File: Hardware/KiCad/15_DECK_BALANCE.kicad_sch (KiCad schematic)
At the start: 0 parts

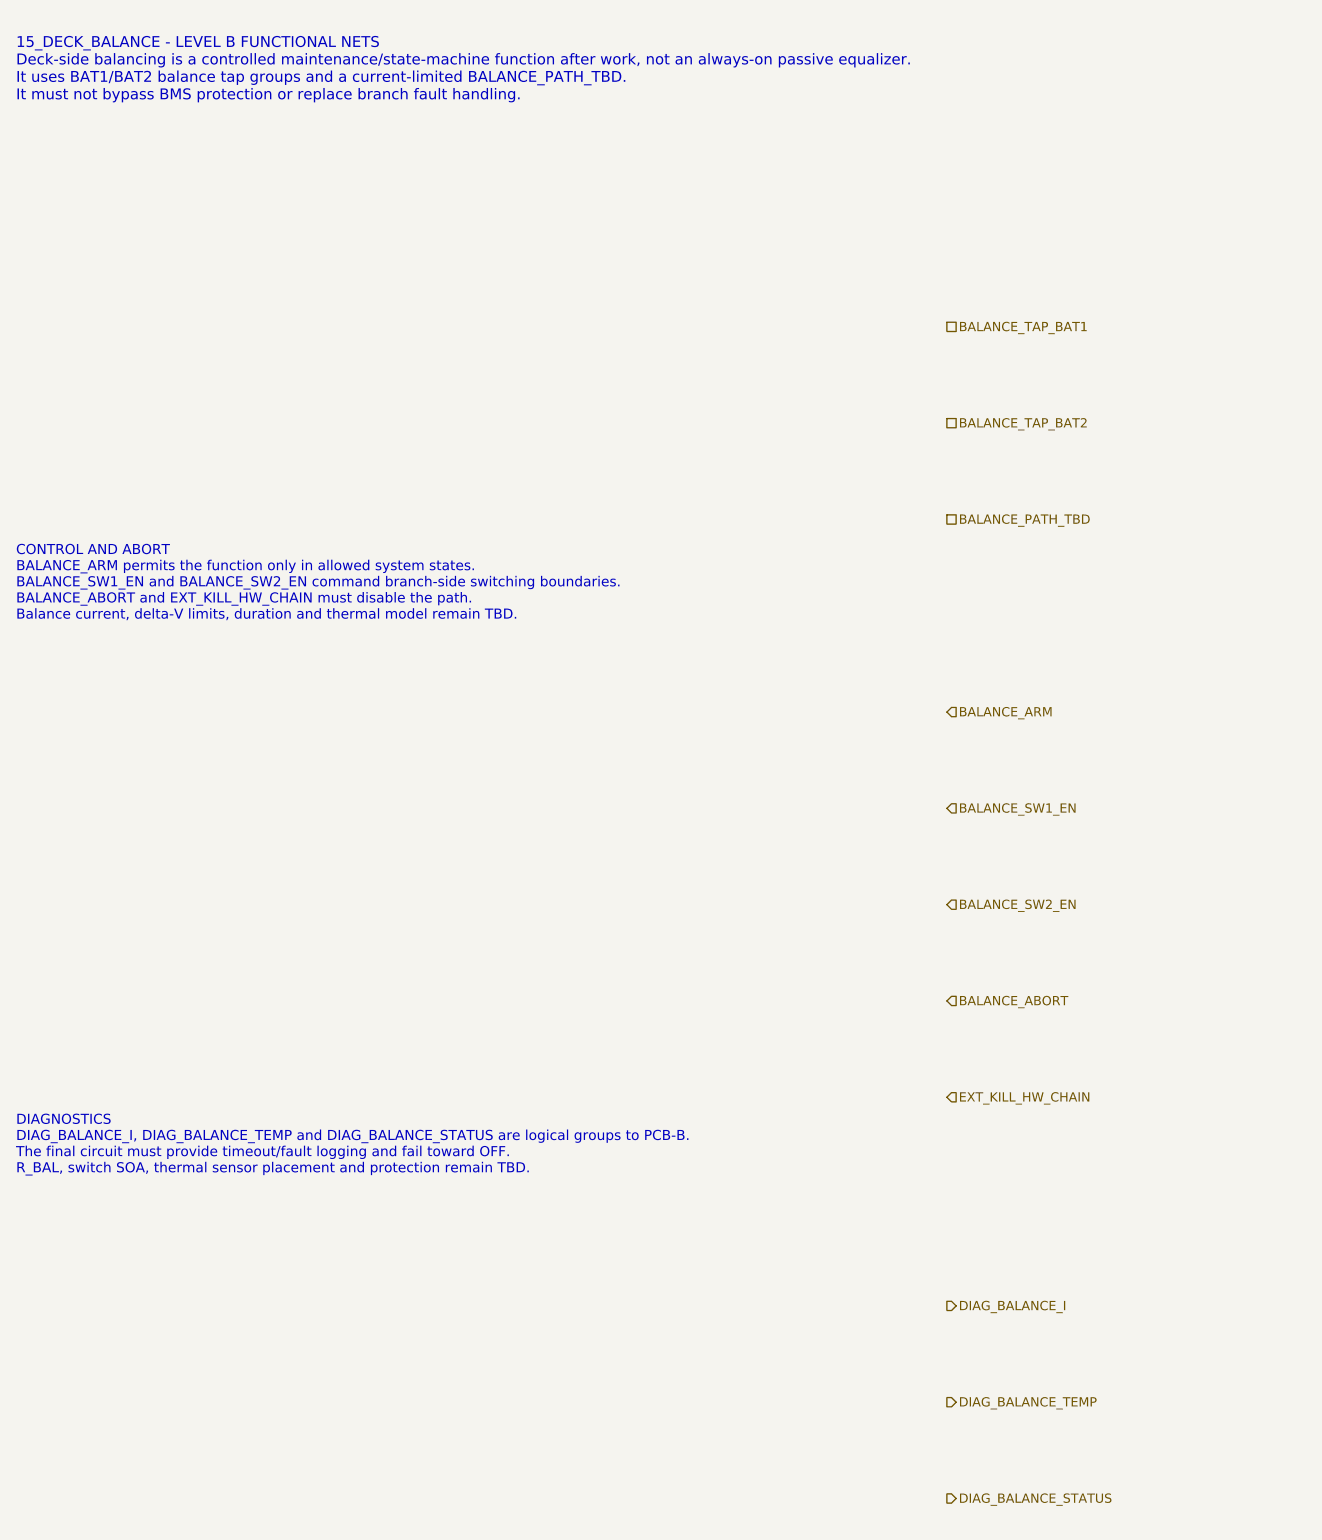
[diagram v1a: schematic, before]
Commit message: hardware: add remaining BFE symbol skeleton zones
Complete text-only symbol skeleton zones for remaining PCB-A BFE_POWER sheets.

Includes PACK_BUS, MAIN paths, measurements, deck balance, connectors and testpoints.
No real KiCad library symbols, part numbers, footprints, BOM entries or PCB layout are introduced.
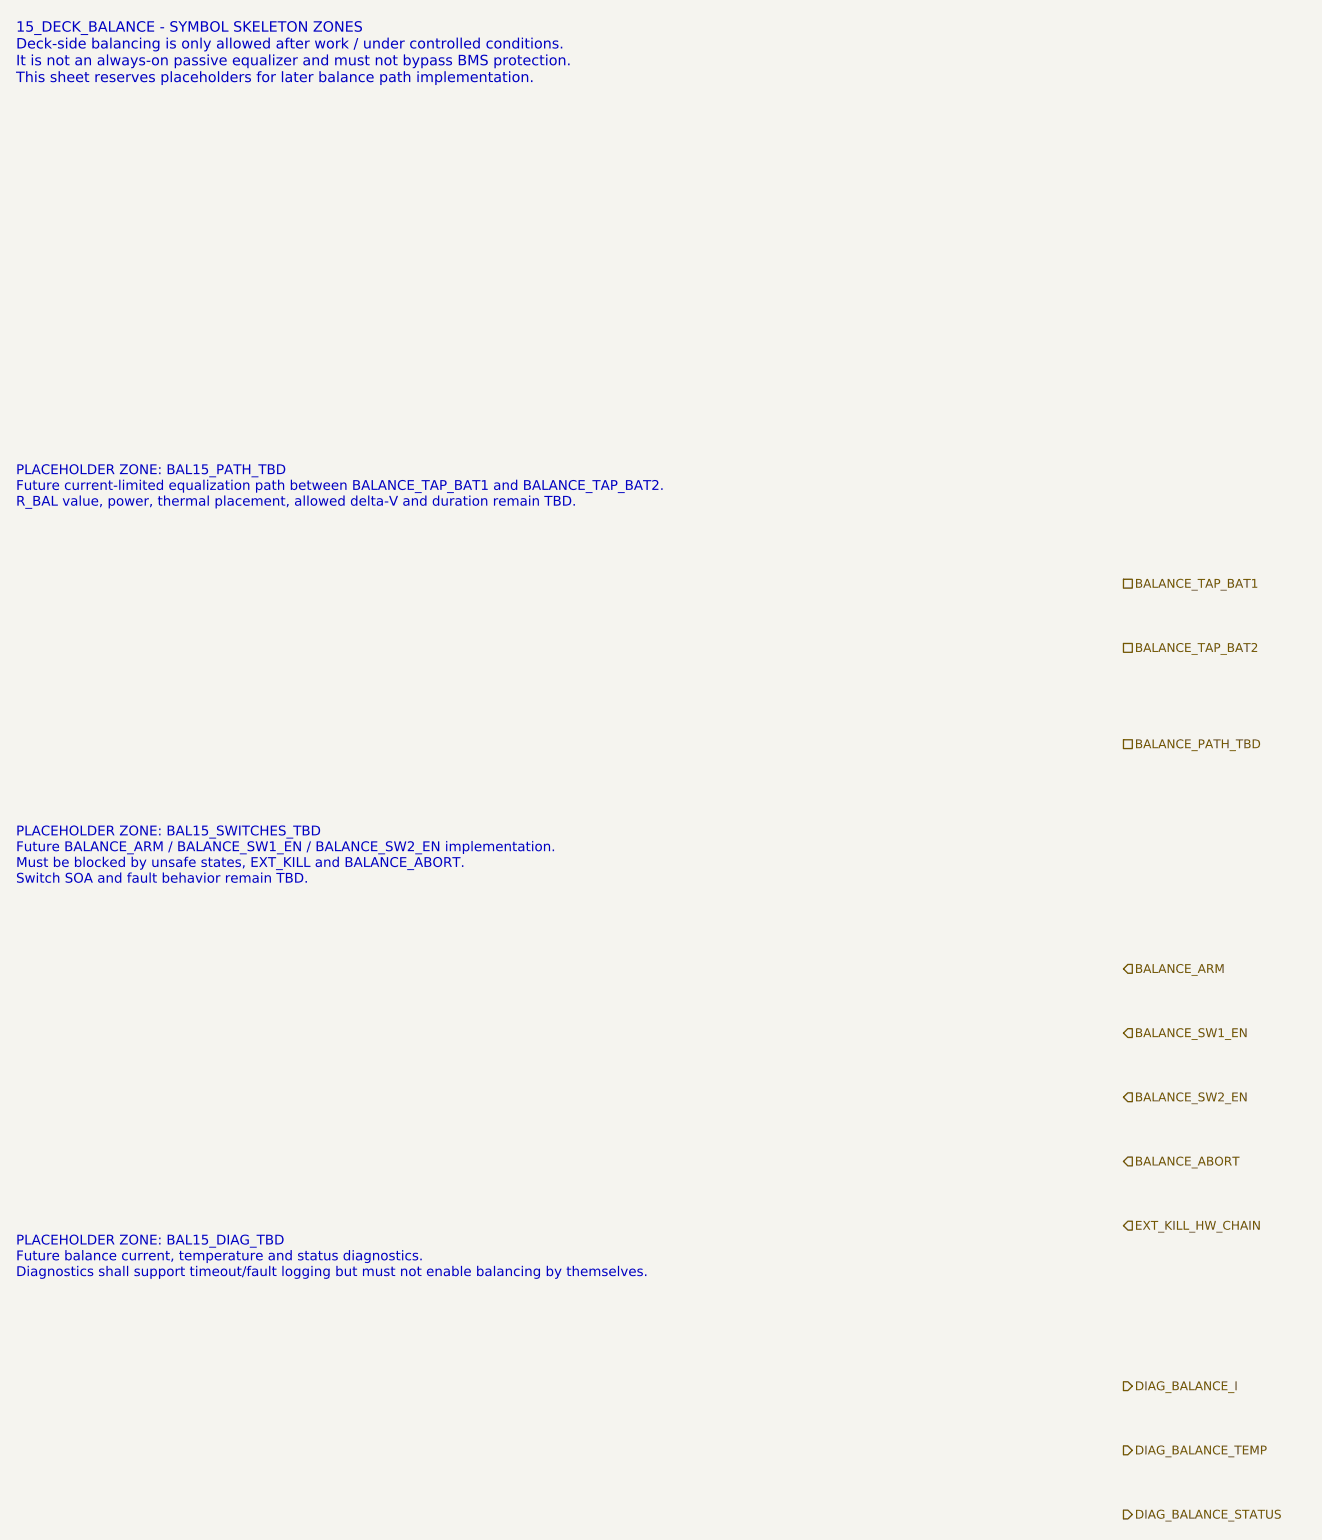
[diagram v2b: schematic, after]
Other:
- note added: "15_DECK_BALANCE - SYMBOL SKELETON ZONES Deck-side balancing is only allowed after work / under controlled conditions. It is not an always-on passive equalizer and must not bypass BMS protection. This sheet reserves placeholders for later balance path implementation."
- note added: "PLACEHOLDER ZONE: BAL15_DIAG_TBD Future balance current, temperature and status diagnostics. Diagnostics shall support timeout/fault logging but must not enable balancing by themselves."
- note added: "PLACEHOLDER ZONE: BAL15_PATH_TBD Future current-limited equalization path between BALANCE_TAP_BAT1 and BALANCE_TAP_BAT2. R_BAL value, power, thermal placement, allowed delta-V and duration remain TBD."
- note added: "PLACEHOLDER ZONE: BAL15_SWITCHES_TBD Future BALANCE_ARM / BALANCE_SW1_EN / BALANCE_SW2_EN implementation. Must be blocked by unsafe states, EXT_KILL and BALANCE_ABORT. Switch SOA and fault behavior remain TBD."
- note removed: "15_DECK_BALANCE - LEVEL B FUNCTIONAL NETS Deck-side balancing is a controlled maintenance/state-machine function after work, not an always-on passive equalizer. It uses BAT1/BAT2 balance tap groups and a current-limited BALANCE_PATH_TBD. It must not bypass BMS protection or replace branch fault handling."
- note removed: "CONTROL AND ABORT BALANCE_ARM permits the function only in allowed system states. BALANCE_SW1_EN and BALANCE_SW2_EN command branch-side switching boundaries. BALANCE_ABORT and EXT_KILL_HW_CHAIN must disable the path. Balance current, delta-V limits, duration and thermal model remain TBD."
- note removed: "DIAGNOSTICS DIAG_BALANCE_I, DIAG_BALANCE_TEMP and DIAG_BALANCE_STATUS are logical groups to PCB-B. The final circuit must provide timeout/fault logging and fail toward OFF. R_BAL, switch SOA, thermal sensor placement and protection remain TBD."
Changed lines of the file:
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@@
 		(title "15_DECK_BALANCE - controlled equalization path")
 		(date "2026-07-15")
-		(rev "B1")
+		(rev "C1")
 		(company "Gonoboben/plataVM")
-		(comment 1 "Architecture Level B: balance control, measurement dependency and abort nets")
-		(comment 2 "No resistor, switch, current value or thermal solution selected")
+		(comment 1 "Symbol skeleton: deck balance switch/resistor/diagnostic placeholders")
+		(comment 2 "No resistor value, switch technology, SOA or footprint selected")
 	)
-	(text "15_DECK_BALANCE - LEVEL B FUNCTIONAL NETS\nDeck-side balancing is a controlled maintenance/state-machine function after work, not an always-on passive equalizer.\nIt uses BAT1/BAT2 balance tap groups and a current-limited BALANCE_PATH_TBD.\nIt must not bypass BMS protection or replace branch fault handling."
+	(text "15_DECK_BALANCE - SYMBOL SKELETON ZONES\nDeck-side balancing is only allowed after work / under controlled conditions.\nIt is not an always-on passive equalizer and must not bypass BMS protection.\nThis sheet reserves placeholders for later balance path implementation."
 		(exclude_from_sim no)
-		(at 12 18 0)
-		(effects (font (size 1.35 1.35)) (justify left))
+		(at 12 16 0)
+		(effects (font (size 1.3 1.3)) (justify left))
 		(uuid "bfe-lb-00000015-0000-4000-8000-000000000101")
 	)
-	(text "CONTROL AND ABORT\nBALANCE_ARM permits the function only in allowed system states.\nBALANCE_SW1_EN and BALANCE_SW2_EN command branch-side switching boundaries.\nBALANCE_ABORT and EXT_KILL_HW_CHAIN must disable the path.\nBalance current, delta-V limits, duration and thermal model remain TBD."
+	(text "PLACEHOLDER ZONE: BAL15_PATH_TBD\nFuture current-limited equalization path between BALANCE_TAP_BAT1 and BALANCE_TAP_BAT2.\nR_BAL value, power, thermal placement, allowed delta-V and duration remain TBD."
 		(exclude_from_sim no)
-		(at 12 82 0)
-		(effects (font (size 1.25 1.25)) (justify left))
+		(at 12 70 0)
+		(effects (font (size 1.22 1.22)) (justify left))
 		(uuid "bfe-lb-00000015-0000-4000-8000-000000000102")
 	)
-	(text "DIAGNOSTICS\nDIAG_BALANCE_I, DIAG_BALANCE_TEMP and DIAG_BALANCE_STATUS are logical groups to PCB-B.\nThe final circuit must provide timeout/fault logging and fail toward OFF.\nR_BAL, switch SOA, thermal sensor placement and protection remain TBD."
+	(text "PLACEHOLDER ZONE: BAL15_SWITCHES_TBD\nFuture BALANCE_ARM / BALANCE_SW1_EN / BALANCE_SW2_EN implementation.\nMust be blocked by unsafe states, EXT_KILL and BALANCE_ABORT.\nSwitch SOA and fault behavior remain TBD."
 		(exclude_from_sim no)
-		(at 12 152 0)
-		(effects (font (size 1.25 1.25)) (justify left))
+		(at 12 116 0)
+		(effects (font (size 1.22 1.22)) (justify left))
 		(uuid "bfe-lb-00000015-0000-4000-8000-000000000103")
 	)
-	(hierarchical_label "BALANCE_TAP_BAT1" (shape passive) (exclude_from_sim no) (at 128 50 0) (effects (font (size 1.15 1.15)) (justify left)) (uuid "bfe-lb-00000015-0000-4000-8000-000000000201"))
-	(hierarchical_label "BALANCE_TAP_BAT2" (shape passive) (exclude_from_sim no) (at 128 62 0) (effects (font (size 1.15 1.15)) (justify left)) (uuid "bfe-lb-00000015-0000-4000-8000-000000000202"))
-	(hierarchical_label "BALANCE_PATH_TBD" (shape passive) (exclude_from_sim no) (at 128 74 0) (effects (font (size 1.15 1.15)) (justify left)) (uuid "bfe-lb-00000015-0000-4000-8000-000000000203"))
-	(hierarchical_label "BALANCE_ARM" (shape input) (exclude_from_sim no) (at 128 98 0) (effects (font (size 1.15 1.15)) (justify left)) (uuid "bfe-lb-00000015-0000-4000-8000-000000000204"))
-	(hierarchical_label "BALANCE_SW1_EN" (shape input) (exclude_from_sim no) (at 128 110 0) (effects (font (size 1.15 1.15)) (justify left)) (uuid "bfe-lb-00000015-0000-4000-8000-000000000205"))
-	(hierarchical_label "BALANCE_SW2_EN" (shape input) (exclude_from_sim no) (at 128 122 0) (effects (font (size 1.15 1.15)) (justify left)) (uuid "bfe-lb-00000015-0000-4000-8000-000000000206"))
-	(hierarchical_label "BALANCE_ABORT" (shape input) (exclude_from_sim no) (at 128 134 0) (effects (font (size 1.15 1.15)) (justify left)) (uuid "bfe-lb-00000015-0000-4000-8000-000000000207"))
-	(hierarchical_label "EXT_KILL_HW_CHAIN" (shape input) (exclude_from_sim no) (at 128 146 0) (effects (font (size 1.15 1.15)) (justify left)) (uuid "bfe-lb-00000015-0000-4000-8000-000000000208"))
-	(hierarchical_label "DIAG_BALANCE_I" (shape output) (exclude_from_sim no) (at 128 172 0) (effects (font (size 1.15 1.15)) (justify left)) (uuid "bfe-lb-00000015-0000-4000-8000-000000000209"))
-	(hierarchical_label "DIAG_BALANCE_TEMP" (shape output) (exclude_from_sim no) (at 128 184 0) (effects (font (size 1.15 1.15)) (justify left)) (uuid "bfe-lb-00000015-0000-4000-8000-000000000210"))
-	(hierarchical_label "DIAG_BALANCE_STATUS" (shape output) (exclude_from_sim no) (at 128 196 0) (effects (font (size 1.15 1.15)) (justify left)) (uuid "bfe-lb-00000015-0000-4000-8000-000000000211"))
+	(text "PLACEHOLDER ZONE: BAL15_DIAG_TBD\nFuture balance current, temperature and status diagnostics.\nDiagnostics shall support timeout/fault logging but must not enable balancing by themselves."
+		(exclude_from_sim no)
+		(at 12 166 0)
+		(effects (font (size 1.22 1.22)) (justify left))
+		(uuid "bfe-lb-00000015-0000-4000-8000-000000000104")
+	)
+	(hierarchical_label "BALANCE_TAP_BAT1" (shape passive) (exclude_from_sim no) (at 150 82 0) (effects (font (size 1.1 1.1)) (justify left)) (uuid "bfe-lb-00000015-0000-4000-8000-000000000201"))
+	(hierarchical_label "BALANCE_TAP_BAT2" (shape passive) (exclude_from_sim no) (at 150 90 0) (effects (font (size 1.1 1.1)) (justify left)) (uuid "bfe-lb-00000015-0000-4000-8000-000000000202"))
+	(hierarchical_label "BALANCE_PATH_TBD" (shape passive) (exclude_from_sim no) (at 150 102 0) (effects (font (size 1.1 1.1)) (justify left)) (uuid "bfe-lb-00000015-0000-4000-8000-000000000203"))
+	(hierarchical_label "BALANCE_ARM" (shape input) (exclude_from_sim no) (at 150 130 0) (effects (font (size 1.1 1.1)) (justify left)) (uuid "bfe-lb-00000015-0000-4000-8000-000000000204"))
+	(hierarchical_label "BALANCE_SW1_EN" (shape input) (exclude_from_sim no) (at 150 138 0) (effects (font (size 1.1 1.1)) (justify left)) (uuid "bfe-lb-00000015-0000-4000-8000-000000000205"))
+	(hierarchical_label "BALANCE_SW2_EN" (shape input) (exclude_from_sim no) (at 150 146 0) (effects (font (size 1.1 1.1)) (justify left)) (uuid "bfe-lb-00000015-0000-4000-8000-000000000206"))
+	(hierarchical_label "BALANCE_ABORT" (shape input) (exclude_from_sim no) (at 150 154 0) (effects (font (size 1.1 1.1)) (justify left)) (uuid "bfe-lb-00000015-0000-4000-8000-000000000207"))
+	(hierarchical_label "EXT_KILL_HW_CHAIN" (shape input) (exclude_from_sim no) (at 150 162 0) (effects (font (size 1.1 1.1)) (justify left)) (uuid "bfe-lb-00000015-0000-4000-8000-000000000208"))
+	(hierarchical_label "DIAG_BALANCE_I" (shape output) (exclude_from_sim no) (at 150 182 0) (effects (font (size 1.1 1.1)) (justify left)) (uuid "bfe-lb-00000015-0000-4000-8000-000000000209"))
+	(hierarchical_label "DIAG_BALANCE_TEMP" (shape output) (exclude_from_sim no) (at 150 190 0) (effects (font (size 1.1 1.1)) (justify left)) (uuid "bfe-lb-00000015-0000-4000-8000-000000000210"))
+	(hierarchical_label "DIAG_BALANCE_STATUS" (shape output) (exclude_from_sim no) (at 150 198 0) (effects (font (size 1.1 1.1)) (justify left)) (uuid "bfe-lb-00000015-0000-4000-8000-000000000211"))
 )
